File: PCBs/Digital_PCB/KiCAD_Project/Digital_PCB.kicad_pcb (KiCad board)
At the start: 4 copper layers, 75 x 84.8 mm, 162 parts, among them J1 NP_Conn_01x02_Relief, J10 HMC Breakout Pins, J11 1-0001555, J12 1-0001555, J13 HMC Breakout Pins, J14 1-0000050, J15 1-0000190, J2 Board to Board, J3 NP_Conn_01x04_Relief, J4 1-0001205, J5 NP_Conn_01x04, J6 NP_Conn_01x02_Relief, J7 NP_Conn_01x04, J8 NP_Conn_01x02_Relief, J9 NP_Conn_01x02_Relief, Q1 1-0001548, Q2 1-0001214, U1 1-0000207, U10 1-0000785, U11 1-0000446, U2 1-0000465, U3 1-0000576, U4 1-0001530, U5 1-0001530, U6 1-0001542, U7 1-0001535, U8 1-0001471, U9 1-0001543, Y1 1-0000721

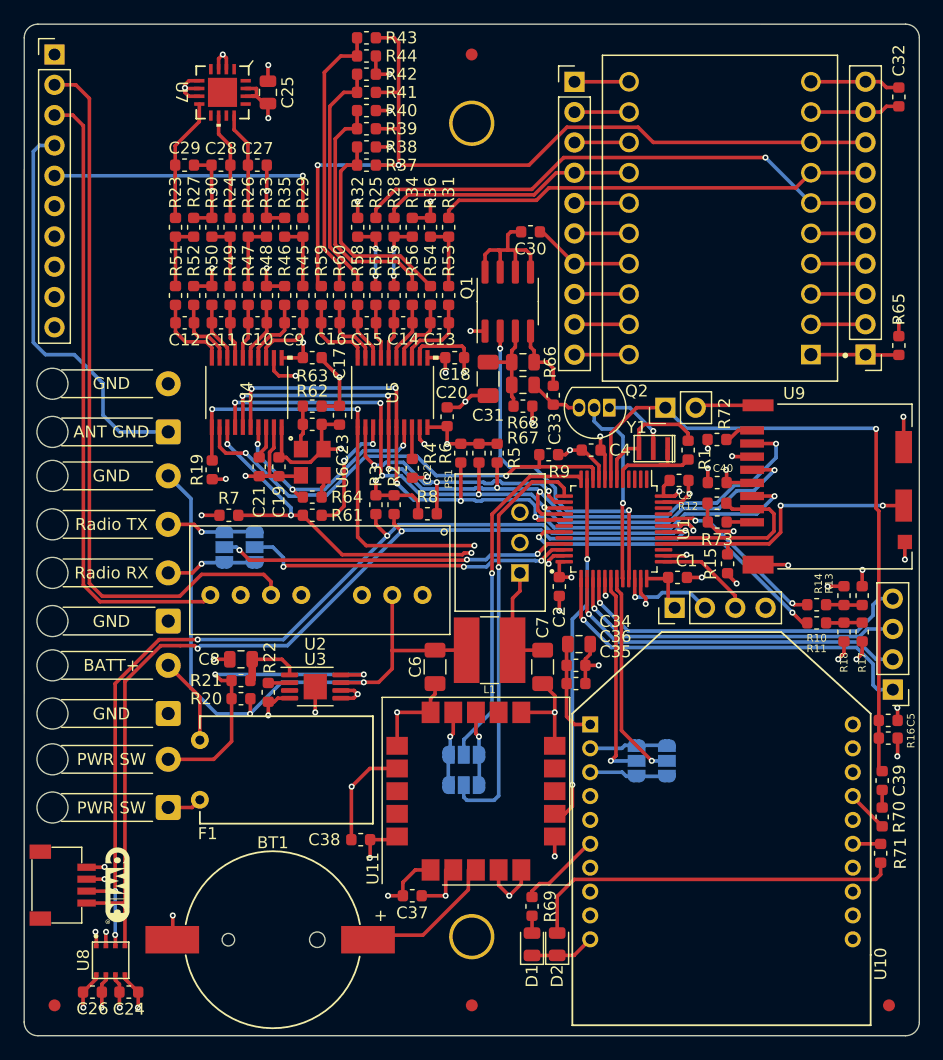
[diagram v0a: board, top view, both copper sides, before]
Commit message: Digital PCB Revisions: Fixed ERC Footprint/Symbol Errors Fixed Remaining ERC Errors Relocated U7 to bottom of PCB
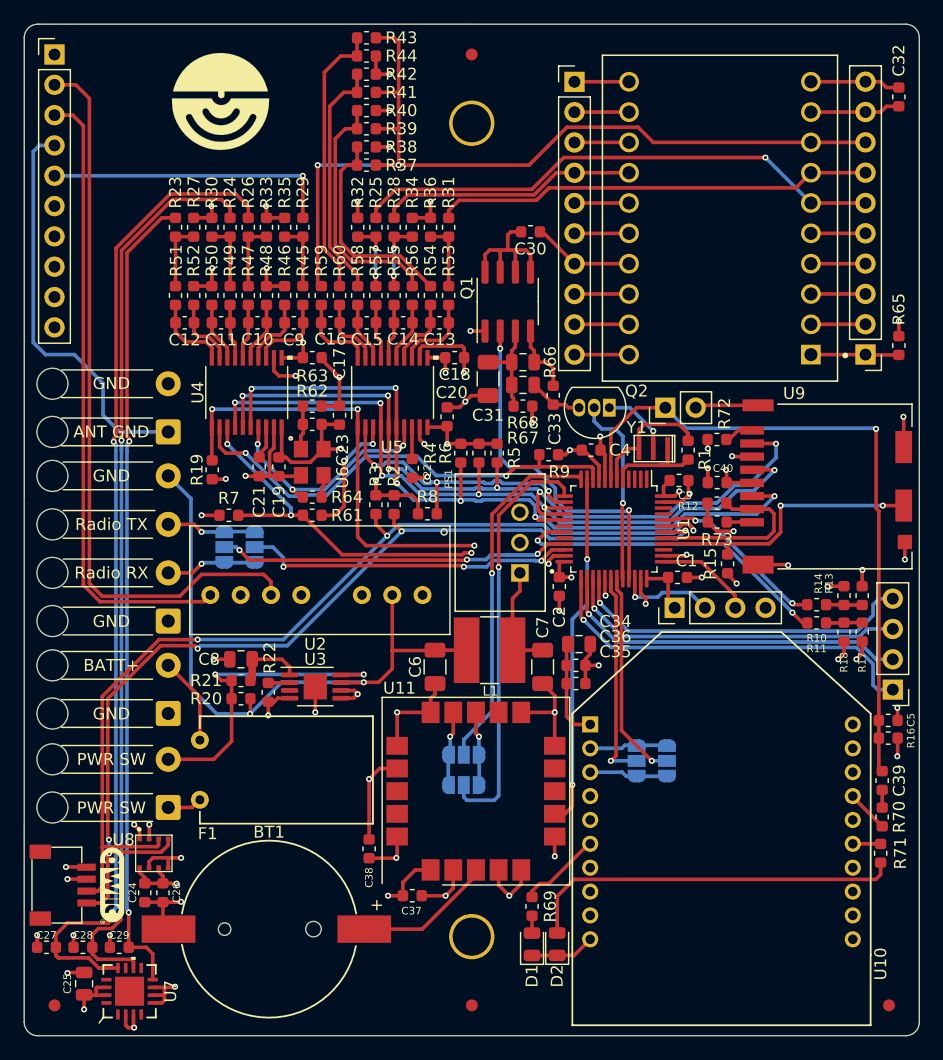
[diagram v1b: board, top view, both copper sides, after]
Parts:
- removed the G*** at (115.8, 129.8)
- added G***: LOGO, pcb_graphics:PCB Logo Standard, F.Cu at (124.3, 64.1)
- added G***: QWIIC, pcb_graphics:5mm qwiic logo, F.Cu at (115.3, 129.8)
- added G***: LOGO, pcb_graphics:PCB Logo Standard, B.Cu at (147.8, 73.3)
- moved C25 76.2 mm to (112.9, 138.0)
- moved U7 75.7 mm to (116.7, 138.7), turned to 90 degrees
- moved C27 67.9 mm to (109.8, 135.0), turned to 180 degrees
- moved C28 66.5 mm to (112.8, 135.0)
- moved C29 65.8 mm to (115.8, 135.0), turned to 180 degrees
- moved C26 10.2 mm to (119.5, 130.4), turned to -90 degrees
- moved U8 9.66 mm to (118.7, 127.1)
- moved C24 8.43 mm to (118.0, 130.4), turned to 90 degrees
- moved C38 1.04 mm to (136.8, 126.7), turned to -90 degrees
- moved BT1 0.94 mm to (128.4, 133.5)
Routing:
- net Xacc: track 9.06 -> 83.5 mm, vias 0 -> 2
- net Yacc: track 8.99 -> 76.9 mm, vias 0 -> 2
- net Zacc: track 10.4 -> 68.1 mm, vias 0 -> 2
- net GND: track 181.5 -> 179.0 mm, vias 52 -> 54
- net +3V3: track 98.4 -> 97.1 mm, vias 24 -> 23
- net I2C_SCL: track 82.0 -> 83.1 mm, vias 3 -> 5
- net I2C_SDA: track 84.4 -> 84.2 mm, vias 5 -> 3
